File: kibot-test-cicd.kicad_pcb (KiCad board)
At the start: 6 copper layers, 47 x 47 mm, 12 parts, among them J1 Conn_02x04_Counter_Clockwise, J2 Conn_01x05_Pin, U1 MT6701CT

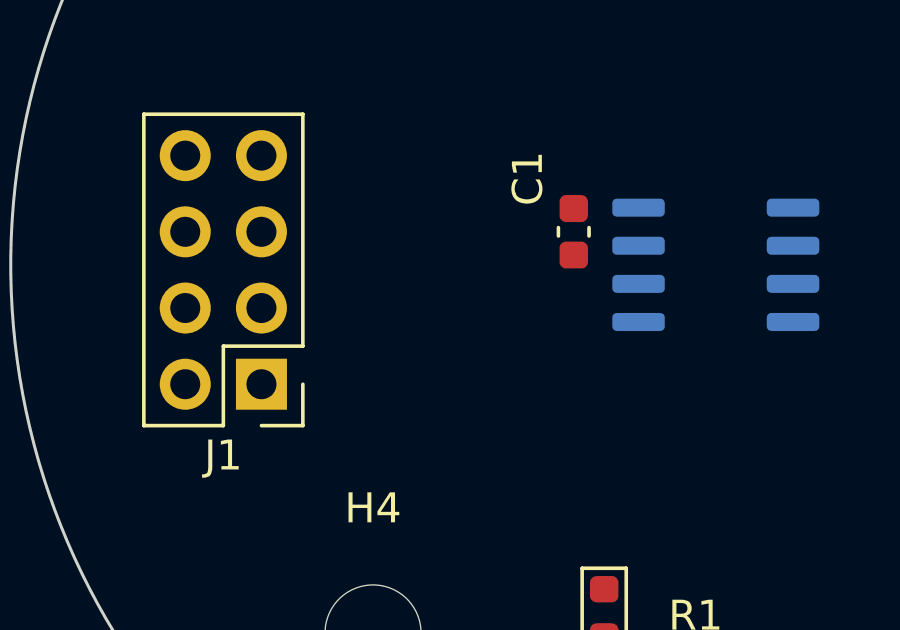
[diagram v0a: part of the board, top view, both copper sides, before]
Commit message: [PCB] added ground plane
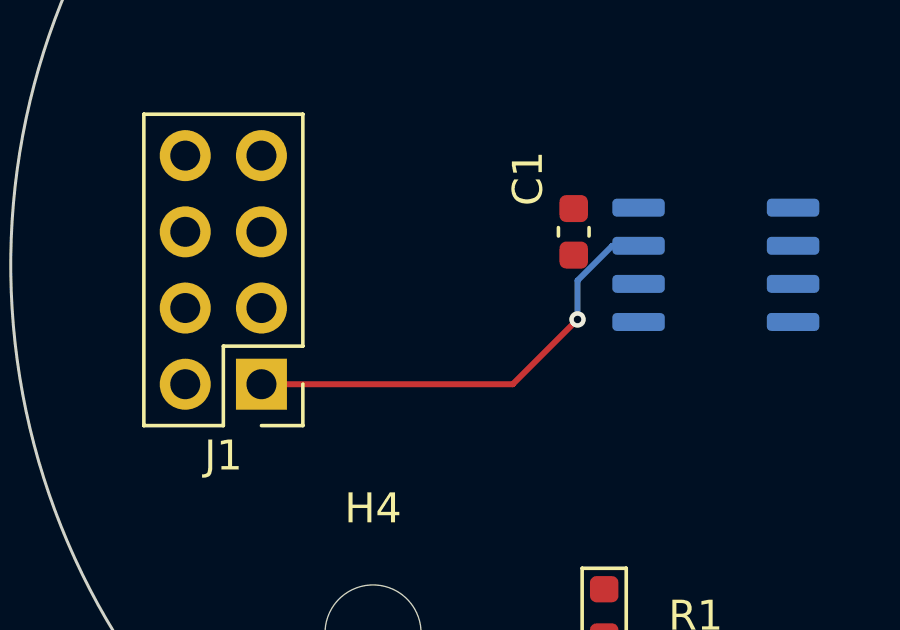
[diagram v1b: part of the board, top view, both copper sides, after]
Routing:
- net out_sel: track 0.00 -> 15.4 mm, vias 0 -> 1
- added copper zone on In1.Cu, net (none)
- added copper zone on In2.Cu, net (none)
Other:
- copper layers 6 -> 4
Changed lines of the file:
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@@
 		(4 "In1.Cu" power "L2 (GND)")
 		(6 "In2.Cu" signal "L3 (Sig, PWR)")
-		(8 "In3.Cu" signal "L4 (Sig, PWR)")
-		(10 "In4.Cu" power "L5 (GND)")
 		(2 "B.Cu" signal "L6 (Sig, PWR)")
 		(9 "F.Adhes" user "F.Adhesive")
@@
 			(layer "F.Mask"
 				(type "Top Solder Mask")
-				(color "Black")
+				(color "Blue")
 				(thickness 0.02)
 				(material "Solder Resist")
@@
 				(type "prepreg")
 				(color "FR4 natural")
-				(thickness 0.18)
+				(thickness 0.1)
 				(material "FR4_7628")
 				(epsilon_r 4.29)
@@
 				(type "core")
 				(color "FR4 natural")
-				(thickness 0.4)
+				(thickness 1.21)
 				(material "FR4")
 				(epsilon_r 4.6)
@@
 				(type "prepreg")
 				(color "FR4 natural")
-				(thickness 0.18)
-				(material "FR4_7628")
-				(epsilon_r 4.29)
-				(loss_tangent 0.02)
-			)
-			(layer "In3.Cu"
-				(type "copper")
-				(thickness 0.035)
-			)
-			(layer "dielectric 4"
-				(type "core")
-				(color "FR4 natural")
-				(thickness 0.4)
-				(material "FR4")
-				(epsilon_r 4.6)
-				(loss_tangent 0.02)
-			)
-			(layer "In4.Cu"
-				(type "copper")
-				(thickness 0.035)
-			)
-			(layer "dielectric 5"
-				(type "prepreg")
-				(color "FR4 natural")
-				(thickness 0.18)
+				(thickness 0.1)
 				(material "FR4_7628")
 				(epsilon_r 4.29)
@@
 			(layer "B.Mask"
 				(type "Bottom Solder Mask")
-				(color "Black")
+				(color "Blue")
 				(thickness 0.02)
 				(material "Solder Resist")
@@
 			)
 		)
+	)
+	(segment
+		(start 141.732 93.98)
+		(end 143.891 91.821)
+		(width 0.2)
+		(layer "F.Cu")
+		(net 4)
+	)
+	(segment
+		(start 144.018 91.694)
+		(end 143.891 91.821)
+		(width 0.2)
+		(layer "F.Cu")
+		(net 4)
+	)
+	(segment
+		(start 133.355 93.98)
+		(end 141.732 93.98)
+		(width 0.2)
+		(layer "F.Cu")
+		(net 4)
+	)
+	(via
+		(at 143.891 91.821)
+		(size 0.55)
+		(drill 0.25)
+		(layers "F.Cu" "B.Cu")
+		(net 4)
+	)
+	(segment
+		(start 143.891 90.524001)
+		(end 143.891 91.821)
+		(width 0.2)
+		(layer "B.Cu")
+		(net 4)
+	)
+	(segment
+		(start 145.925 89.365)
+		(end 145.050001 89.365)
+		(width 0.2)
+		(layer "B.Cu")
+		(net 4)
+	)
+	(segment
+		(start 145.050001 89.365)
+		(end 143.891 90.524001)
+		(width 0.2)
+		(layer "B.Cu")
+		(net 4)
+	)
+	(zone
+		(net 0)
+		(net_name "")
+		(layers "In1.Cu" "In2.Cu")
+		(hatch edge 0.5)
+		(connect_pads
+			(clearance 0)
+		)
+		(min_thickness 0.25)
+		(filled_areas_thickness no)
+		(fill yes
+			(thermal_gap 0.5)
+			(thermal_bridge_width 0.5)
+			(island_removal_mode 1)
+			(island_area_min 10)
+		)
+		(polygon
+			(pts
+				(xy 123.952 67.31) (xy 123.952 114.554) (xy 172.72 114.554) (xy 174.752 112.522) (xy 174.752 67.818)
+				(xy 172.72 65.786) (xy 125.476 65.786)
+			)
+		)

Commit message: [PCB] finished layout
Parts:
- moved JP1 8.80 mm to (150.0, 97.5), turned to 180 degrees
- moved R1 7.33 mm to (146.1, 95.8), turned to -90 degrees
- moved D2 7.13 mm to (144.3, 94.5)
- moved C1 4.51 mm to (146.0, 92.8), turned to 90 degrees
- moved H2 1.95 mm to (160.5, 102.0)
- moved H3 1.82 mm to (160.5, 78.0)
- moved J1 0.76 mm to (134.1, 94.0)
- moved H1 0.71 mm to (136.5, 78.0)
- moved H4 0.64 mm to (136.5, 102.0)
- moved D1 0.61 mm to (160.2, 90.4), turned to 0 degrees
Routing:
- net Z-CS: track 0.00 -> 40.1 mm, vias 0 -> 3
- net +3V3: track 0.00 -> 35.3 mm, vias 0 -> 1
- net SDA-A: track 0.00 -> 32.9 mm, vias 0 -> 1
- net SCL-B: track 0.00 -> 32.7 mm, vias 0 -> 3
- net push: track 0.00 -> 30.7 mm, vias 0 -> 2
- net mode: track 0.00 -> 18.1 mm, vias 0 -> 1
- net GND: track 0.00 -> 6.21 mm, vias 0 -> 5
- net Net-(JP1-B): track 0.00 -> 3.80 mm
- net Net-(D2-A): track 0.00 -> 1.79 mm
- net out_sel: track 15.4 -> 13.7 mm
- added copper zone on B.Cu, net GND
- added copper zone on F.Cu, net GND
- removed copper zone on In1.Cu, net (none)
- removed copper zone on In2.Cu, net (none)
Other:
- board size 47 x 47 mm -> 40 x 40 mm
- copper layers 4 -> 2

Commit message: minor adjustments
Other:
- board text added: "4x M3"
- board text added: "R 20"

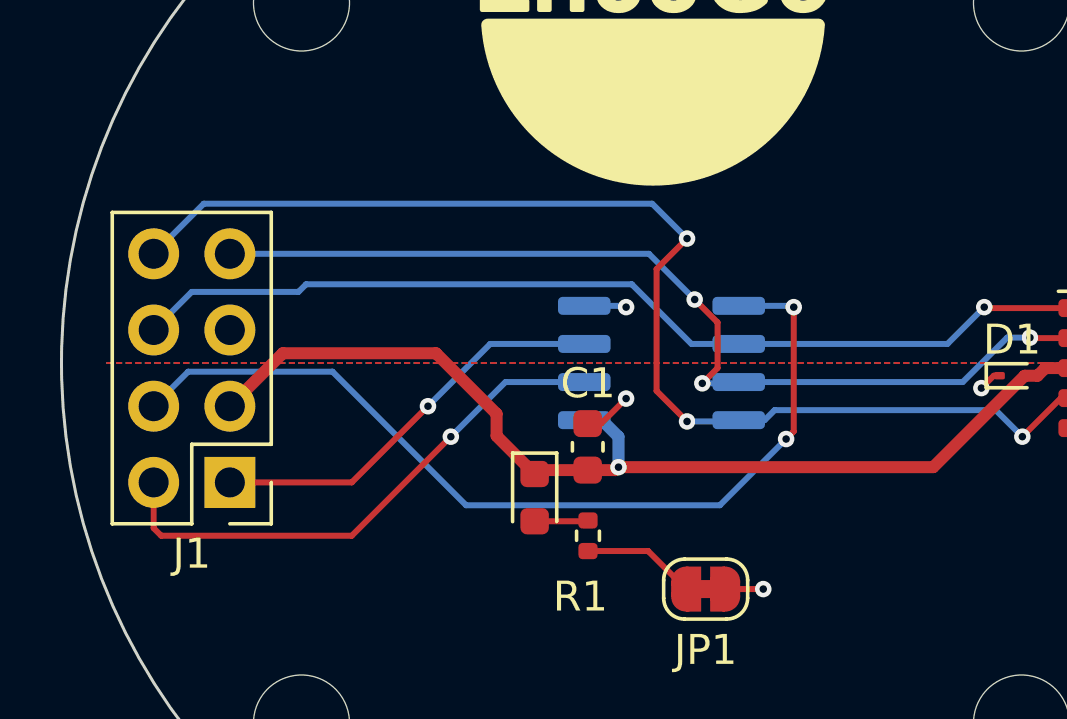
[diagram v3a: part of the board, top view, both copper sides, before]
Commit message: DRC violations fixed
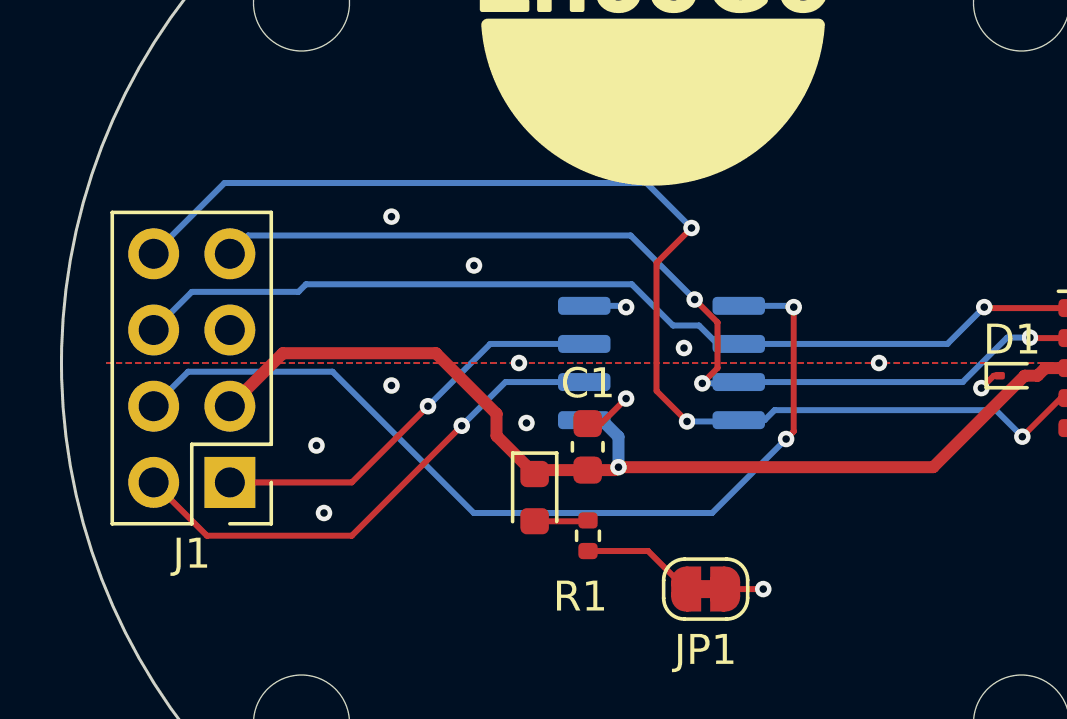
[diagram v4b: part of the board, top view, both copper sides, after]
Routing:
- net Z-CS: track 40.1 -> 41.1 mm
- net mode: track 18.1 -> 17.2 mm
- net SCL-B: track 32.7 -> 33.2 mm
- net GND: vias 5 -> 14

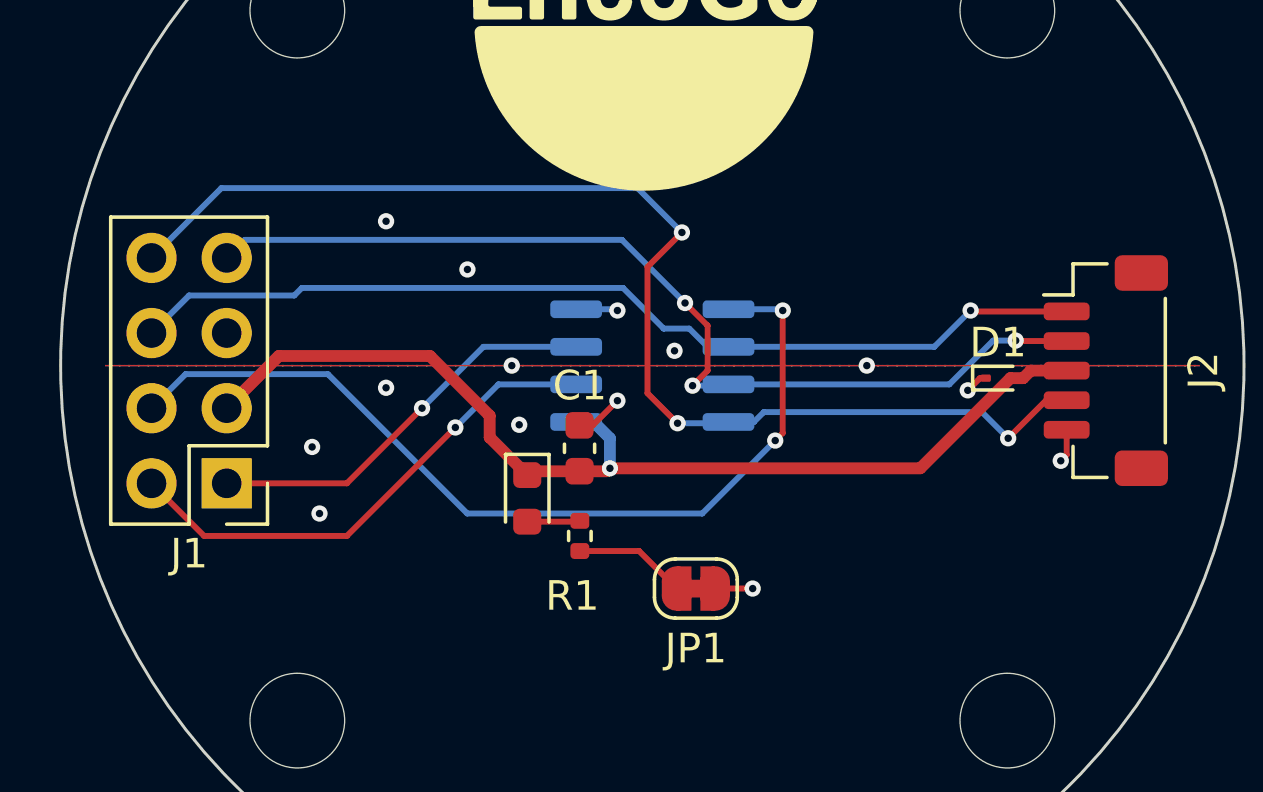
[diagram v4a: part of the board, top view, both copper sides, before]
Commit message: fixed the via sizes to match the HERL capabilities
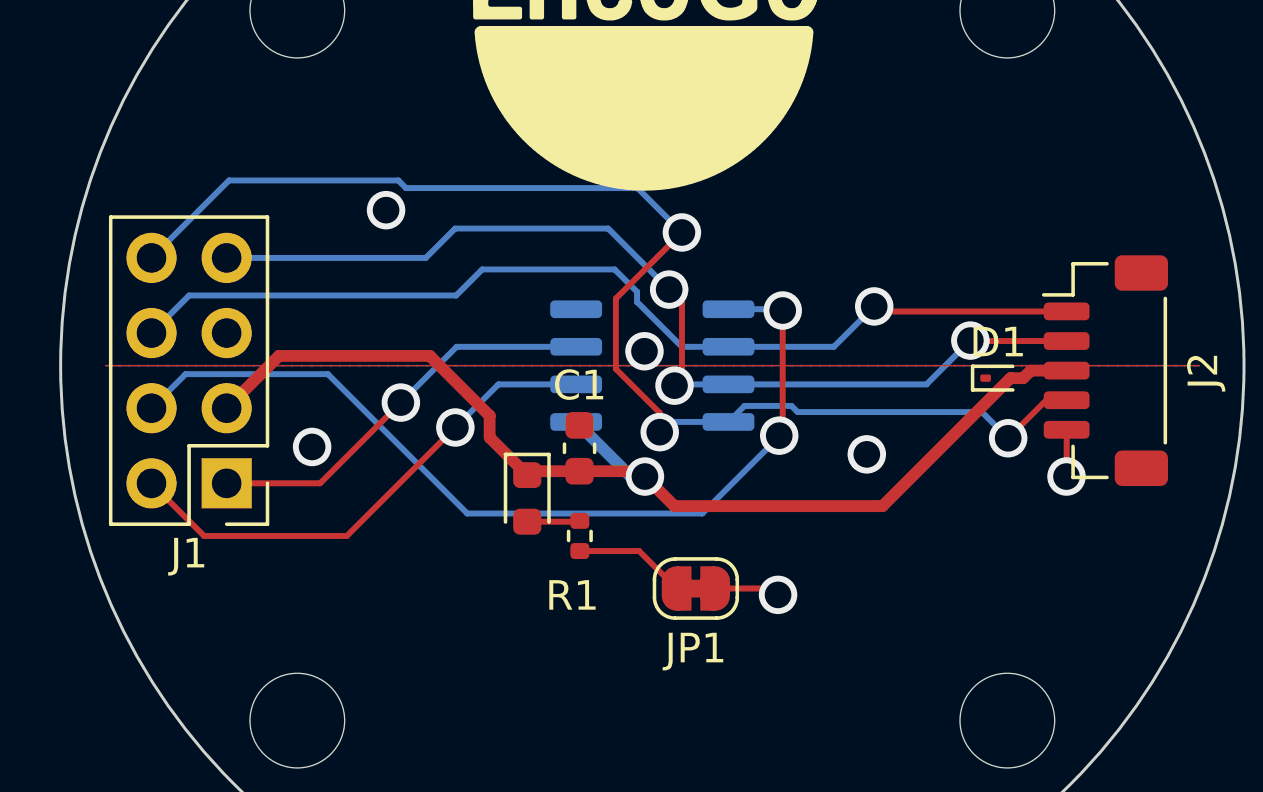
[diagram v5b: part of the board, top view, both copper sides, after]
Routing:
- net GND: track 6.21 -> 3.80 mm, vias 14 -> 6
- net Z-CS: track 41.1 -> 43.1 mm
- net +3V3: track 35.3 -> 37.0 mm
- net SDA-A: track 32.9 -> 33.7 mm

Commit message: added dimensions to back of board for encoder height
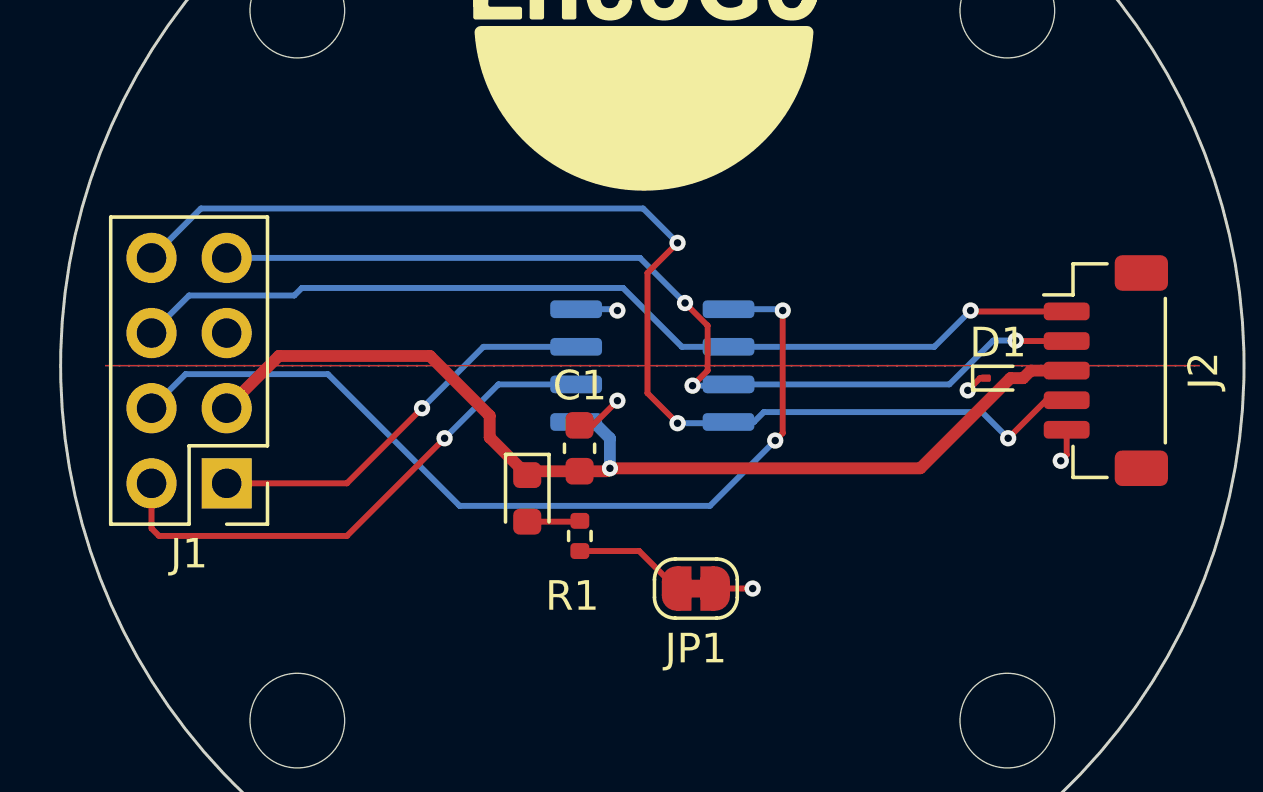
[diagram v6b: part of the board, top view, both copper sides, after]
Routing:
- net Z-CS: track 43.1 -> 40.1 mm
- net GND: track 3.80 -> 6.21 mm, vias 6 -> 5
- net +3V3: track 37.0 -> 35.3 mm
- net SCL-B: track 33.6 -> 32.7 mm
- net mode: track 17.2 -> 18.1 mm
- net SDA-A: track 33.7 -> 32.9 mm
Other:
- board text added: "z = 1.45mm Min - 1.75mm Max"
- board text removed: "30°"
- board text removed: "3× 120°"
